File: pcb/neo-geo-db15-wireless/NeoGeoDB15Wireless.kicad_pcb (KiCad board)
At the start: 2 copper layers, 39.9 x 32 mm, 5 parts, among them J1 DB15_F, U1 RP2040-Zero, U2 NRF24L01

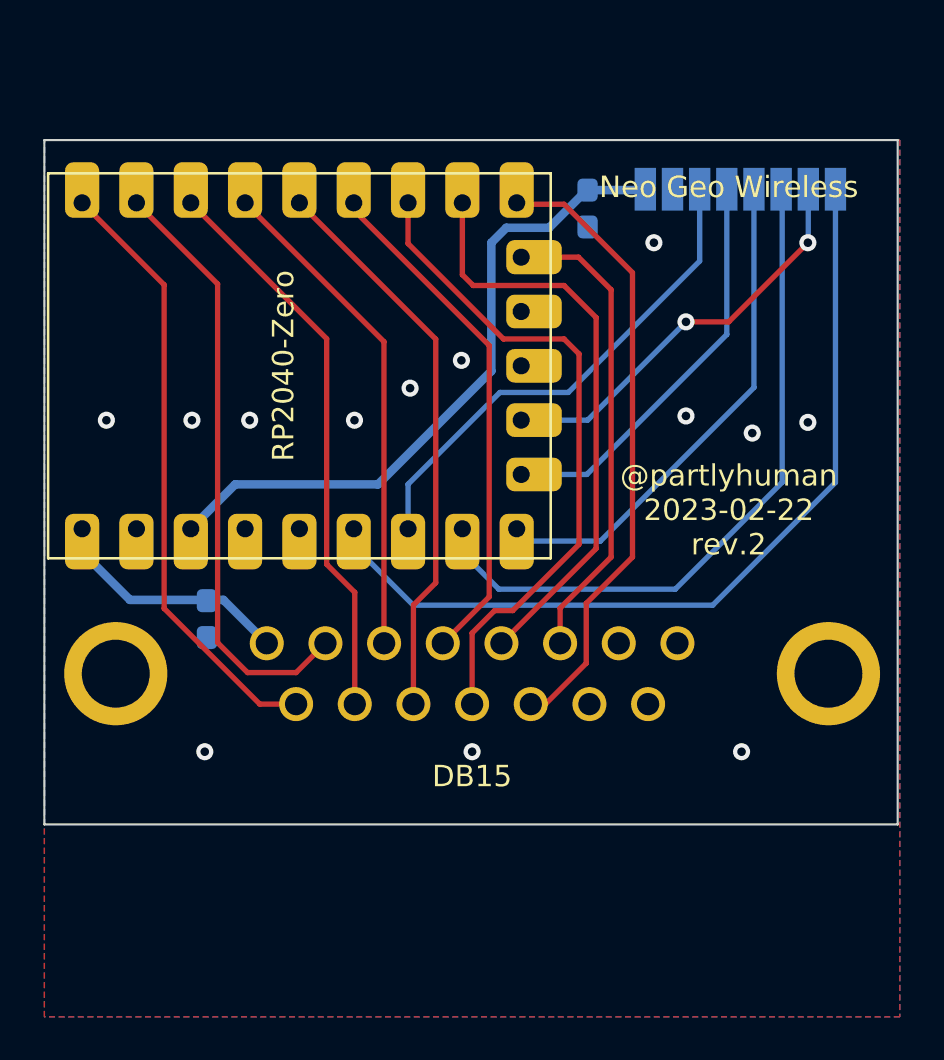
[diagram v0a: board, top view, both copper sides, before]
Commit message: Adds resistor packs for current limiting on button lines
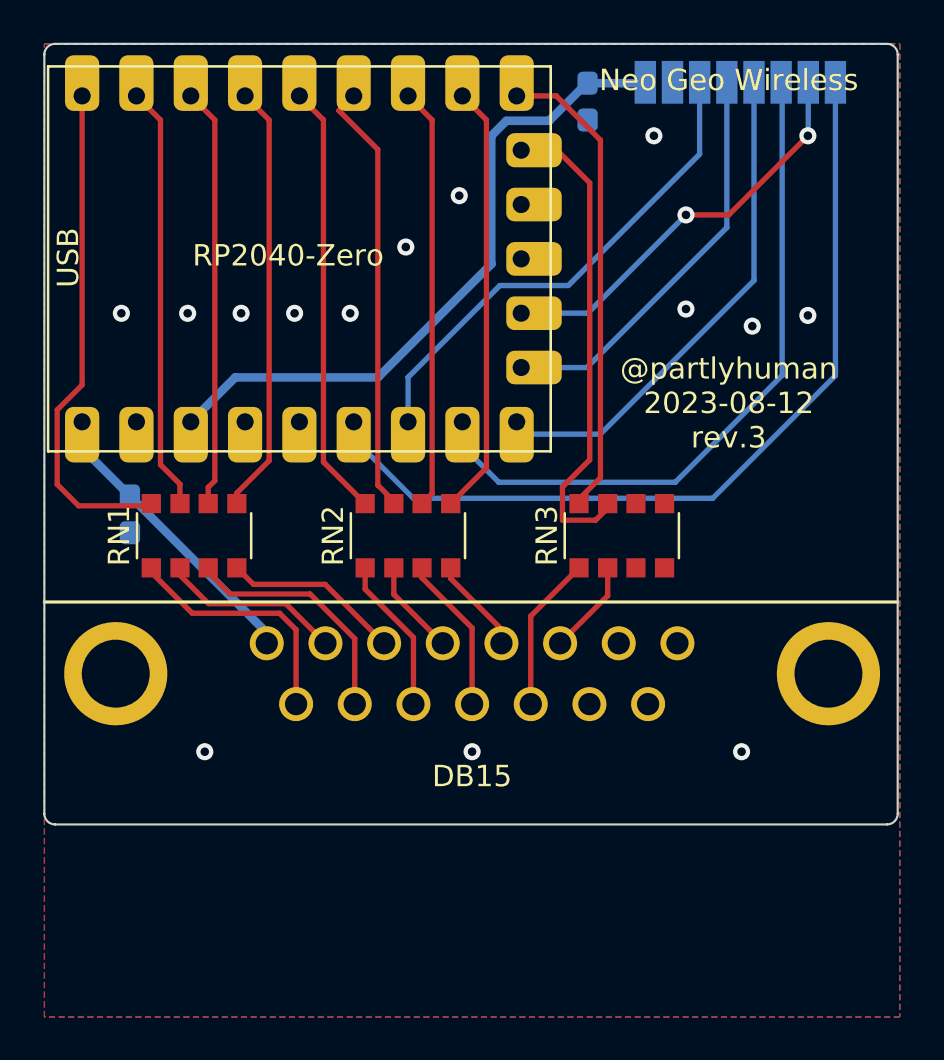
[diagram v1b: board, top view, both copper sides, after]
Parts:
- added RN1: R_Pack04, Resistor_SMD:R_Array_Convex_4x1206, F.Cu at (87.0, 80.0)
- added RN2: R_Pack04, Resistor_SMD:R_Array_Convex_4x1206, F.Cu at (97.0, 80.0)
- added RN3: R_Pack04, Resistor_SMD:R_Array_Convex_4x1206, F.Cu at (107.0, 80.0)
- moved C1 6.08 mm to (84.0, 79.0)
- moved C2 5.00 mm to (105.4, 59.7)
- moved U1 5.00 mm to (104.6, 77.2)
- moved U2 5.00 mm to (112.5, 67.5)
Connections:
- J1 pad 11: /STA -> /STA_IN
- J1 pad 12: /BC -> /BC_IN
- J1 pad 13: /BA -> /BA_IN
- J1 pad 14: /DL -> /DL_IN
- J1 pad 15: /DU -> /DU_IN
- J1 pad 3: /SEL -> /SEL_IN
- J1 pad 4: /BD -> /BD_IN
- J1 pad 5: /BB -> /BB_IN
- J1 pad 6: /DR -> /DR_IN
- J1 pad 7: /DD -> /DD_IN
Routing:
- net /DU_IN: track 0.00 -> 11.6 mm
- net /DL_IN: track 0.00 -> 11.4 mm
- net /BC: track 31.0 -> 19.7 mm
- net /DD_IN: track 0.00 -> 8.46 mm
- net /DD: track 28.3 -> 19.9 mm
- net /DR_IN: track 0.00 -> 8.35 mm
- net /BC_IN: track 0.00 -> 7.34 mm
- net /BA_IN: track 0.00 -> 7.31 mm
- net /STA_IN: track 0.00 -> 7.31 mm
- net /BD: track 27.5 -> 20.2 mm
- net /STA: track 29.3 -> 22.2 mm
- net /DL: track 26.6 -> 19.7 mm
- net /BA: track 26.5 -> 20.3 mm
- net /DU: track 28.6 -> 23.5 mm
- net /BD_IN: track 0.00 -> 4.51 mm
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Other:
- board size 39.9 x 32 mm -> 39.9 x 36.5 mm
- board text added: "USB"

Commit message: Add JLCJLCJLCJLC
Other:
- board text added: "JLCJLCJLCJLC"
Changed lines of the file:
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@@
     (effects (font (size 1 1) (thickness 0.15)))
+  )
+  (gr_text "JLCJLCJLCJLC" (at 80.8 92.9) (layer "F.SilkS")
+    (effects (font (size 0.8 0.8) (thickness 0.15)) (justify left bottom))
   )
   (gr_text "USB" (at 81.7 67 90) (layer "F.SilkS")

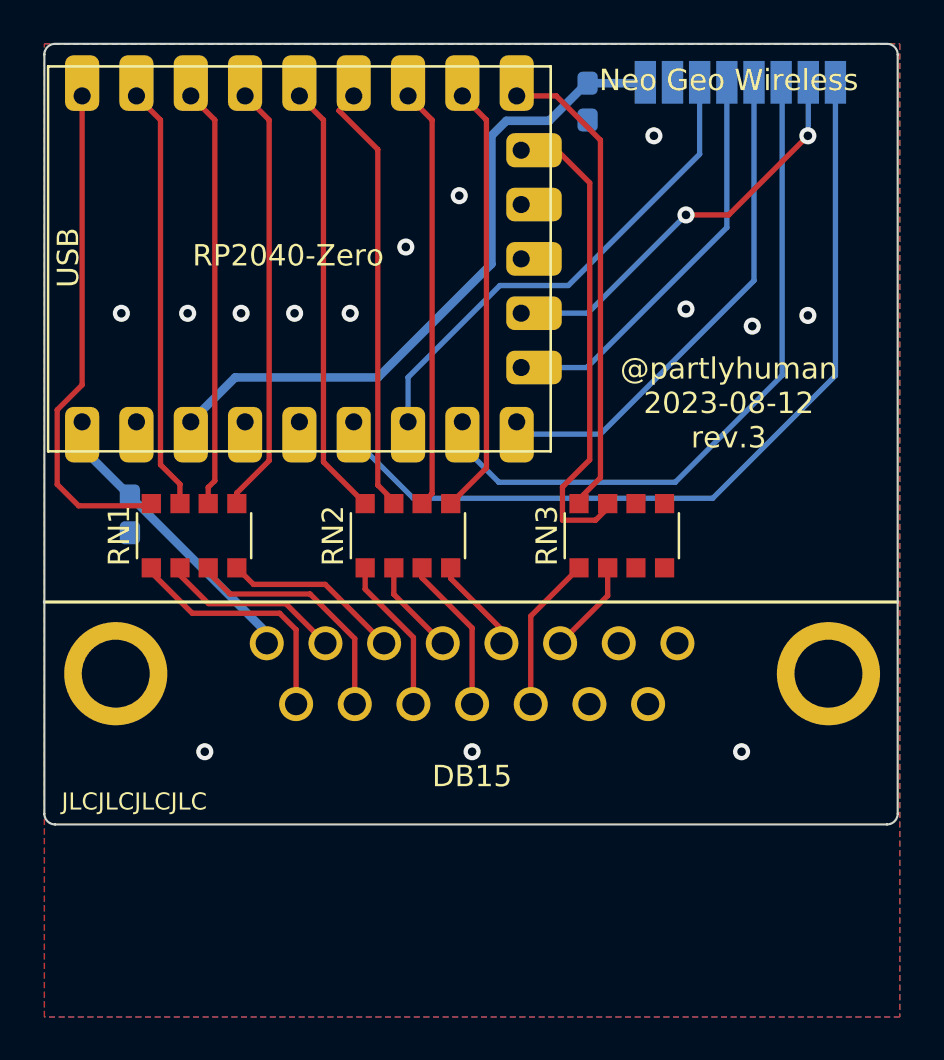
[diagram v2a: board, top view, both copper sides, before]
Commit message: Round size up to 40mm
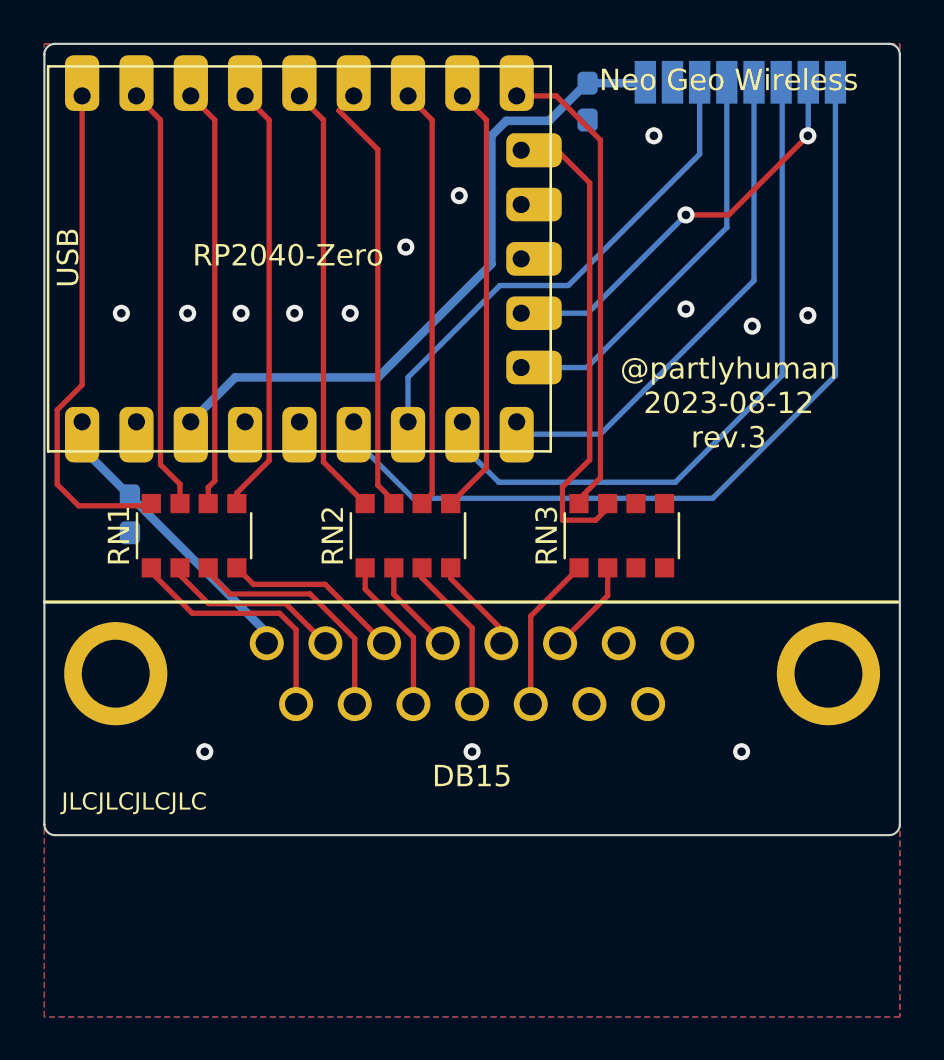
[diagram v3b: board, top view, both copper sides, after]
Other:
- board size 39.9 x 36.5 mm -> 40 x 37 mm
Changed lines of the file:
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@@
   (gr_line (start 80 83.1) (end 119.9 83.1)
     (stroke (width 0.15) (type default)) (layer "F.SilkS"))
-  (gr_arc (start 119.4 57) (mid 119.753553 57.146447) (end 119.9 57.5)
+  (gr_line (start 80.5 57) (end 119.5 57)
     (stroke (width 0.1) (type default)) (layer "Edge.Cuts"))
-  (gr_line (start 119.9 57.5) (end 119.9 93)
+  (gr_line (start 80 93.5) (end 80 57.5)
+    (stroke (width 0.1) (type default)) (layer "Edge.Cuts"))
+  (gr_line (start 119.5 94) (end 80.5 94)
     (stroke (width 0.1) (type default)) (layer "Edge.Cuts"))
   (gr_arc (start 80 57.5) (mid 80.146447 57.146447) (end 80.5 57)
     (stroke (width 0.1) (type default)) (layer "Edge.Cuts"))
-  (gr_arc (start 119.9 93) (mid 119.753553 93.353553) (end 119.4 93.5)
+  (gr_line (start 120 57.5) (end 120 93.5)
     (stroke (width 0.1) (type default)) (layer "Edge.Cuts"))
-  (gr_arc (start 80.5 93.5) (mid 80.146447 93.353553) (end 80 93)
+  (gr_arc (start 119.5 57) (mid 119.853553 57.146447) (end 120 57.5)
     (stroke (width 0.1) (type default)) (layer "Edge.Cuts"))
-  (gr_line (start 80 93) (end 80 57.5)
+  (gr_arc (start 120 93.5) (mid 119.853553 93.853553) (end 119.5 94)
     (stroke (width 0.1) (type default)) (layer "Edge.Cuts"))
-  (gr_line (start 119.4 93.5) (end 80.5 93.5)
-    (stroke (width 0.1) (type default)) (layer "Edge.Cuts"))
-  (gr_line (start 80.5 57) (end 119.4 57)
+  (gr_arc (start 80.5 94) (mid 80.146447 93.853553) (end 80 93.5)
     (stroke (width 0.1) (type default)) (layer "Edge.Cuts"))
   (gr_text "DB15" (at 100 91.25) (layer "F.SilkS")

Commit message: Voltage dividers on button inputs for pico safety
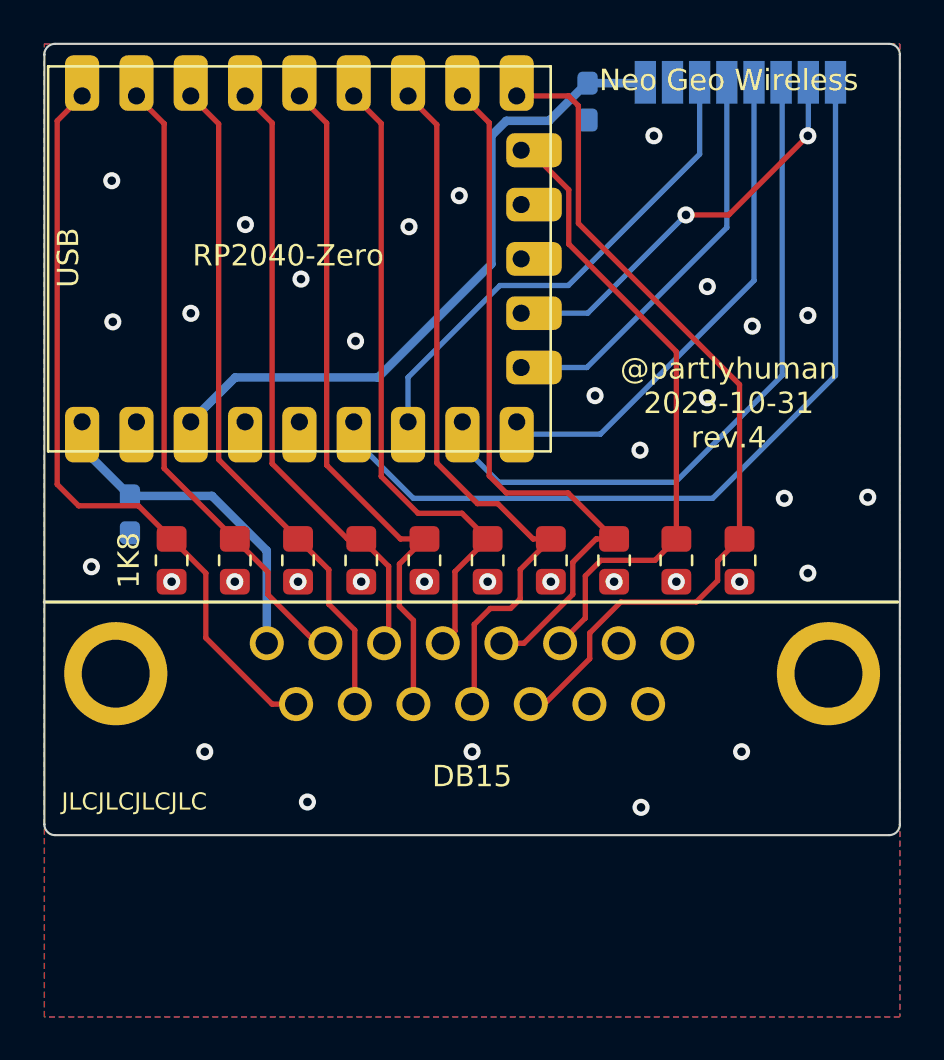
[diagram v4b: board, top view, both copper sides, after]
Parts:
- removed RN1, RN2, RN3: R_Pack04, Resistor_SMD:R_Array_Convex_4x1206
- added R1: 1K8, Resistor_SMD:R_0805_2012Metric_Pad1.20x1.40mm_HandSolder, F.Cu at (86.0, 81.2)
- added R10: 1K8, Resistor_SMD:R_0805_2012Metric_Pad1.20x1.40mm_HandSolder, F.Cu at (109.5, 81.2)
- added R2: 1K8, Resistor_SMD:R_0805_2012Metric_Pad1.20x1.40mm_HandSolder, F.Cu at (88.9, 81.2)
- added R3: 1K8, Resistor_SMD:R_0805_2012Metric_Pad1.20x1.40mm_HandSolder, F.Cu at (91.9, 81.2)
- added R4: 1K8, Resistor_SMD:R_0805_2012Metric_Pad1.20x1.40mm_HandSolder, F.Cu at (94.8, 81.2)
- added R5: 1K8, Resistor_SMD:R_0805_2012Metric_Pad1.20x1.40mm_HandSolder, F.Cu at (97.8, 81.2)
- added R6: 1K8, Resistor_SMD:R_0805_2012Metric_Pad1.20x1.40mm_HandSolder, F.Cu at (100.7, 81.2)
- added R7: 1K8, Resistor_SMD:R_0805_2012Metric_Pad1.20x1.40mm_HandSolder, F.Cu at (103.7, 81.2)
- added R8: 1K8, Resistor_SMD:R_0805_2012Metric_Pad1.20x1.40mm_HandSolder, F.Cu at (106.6, 81.2)
- added R9: 1K8, Resistor_SMD:R_0805_2012Metric_Pad1.20x1.40mm_HandSolder, F.Cu at (112.5, 81.2)
- U2: value NRF24L01 -> NRF24L01_Breakout
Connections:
- J1 pad 11: /STA_IN -> /STA
- J1 pad 12: /BC_IN -> /BC
- J1 pad 13: /BA_IN -> /BA
- J1 pad 14: /DL_IN -> /DL
- J1 pad 15: /DU_IN -> /DU
- J1 pad 3: /SEL_IN -> /SEL
- J1 pad 4: /BD_IN -> /BD
- J1 pad 5: /BB_IN -> /BB
- J1 pad 6: /DR_IN -> /DR
- J1 pad 7: /DD_IN -> /DD
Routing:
- net /STA: track 22.2 -> 40.7 mm
- net /BC: track 19.7 -> 34.3 mm
- net /BD: track 20.2 -> 33.5 mm
- net /DU: track 23.5 -> 35.8 mm
- net /DL: track 19.7 -> 31.6 mm
- net /BA: track 20.3 -> 32.3 mm
- net /DU_IN: track 11.6 -> 0.00 mm
- net /DL_IN: track 11.4 -> 0.00 mm
- net /BB: track 20.4 -> 30.3 mm
- net /DD: track 19.9 -> 29.5 mm
- net /DR: track 20.2 -> 28.8 mm
- net /DD_IN: track 8.46 -> 0.00 mm
- net /DR_IN: track 8.35 -> 0.00 mm
- net /BC_IN: track 7.34 -> 0.00 mm
- net /SEL: track 22.7 -> 30.0 mm
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
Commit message: Rev4 wireless board with voltage dividers
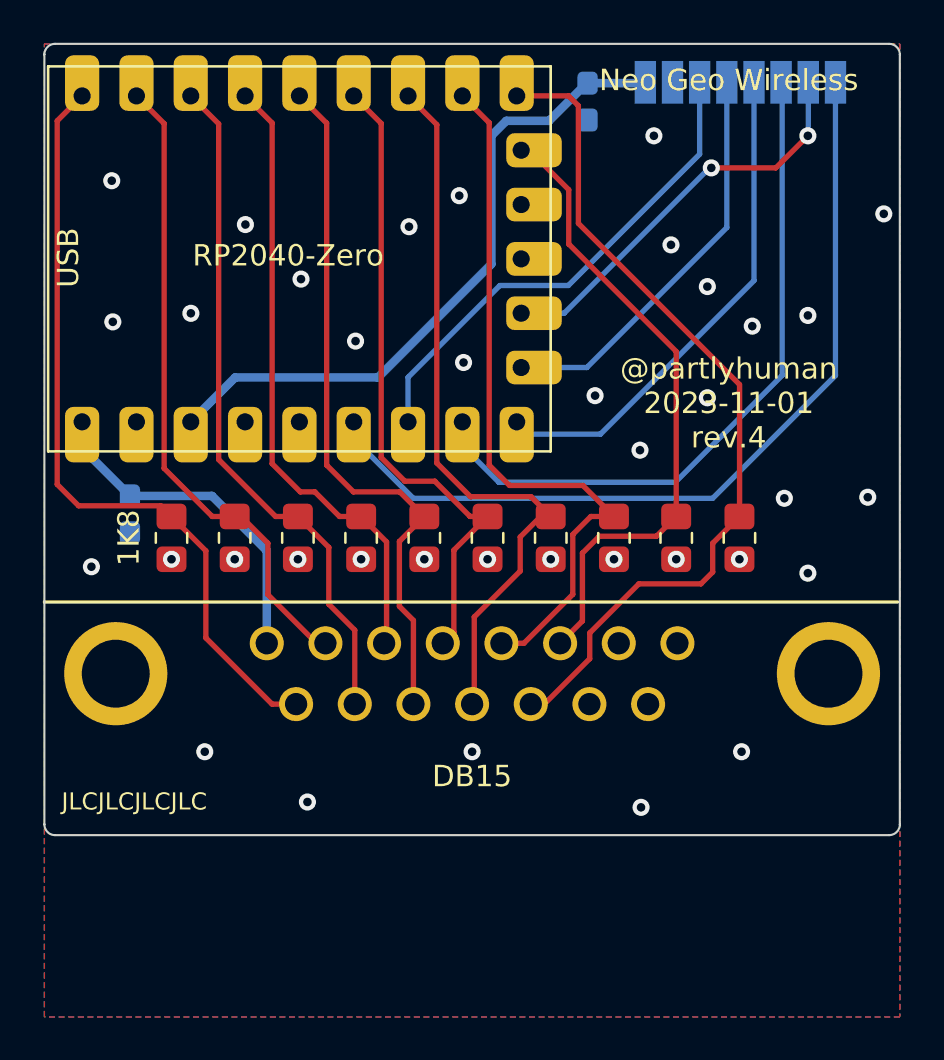
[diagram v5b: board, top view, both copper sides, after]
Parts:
- moved R1 1.05 mm to (85.9, 80.1)
- moved R10 1.05 mm to (109.5, 80.1)
- moved R2 1.05 mm to (88.9, 80.1)
- moved R3 1.05 mm to (91.9, 80.1)
- moved R4 1.05 mm to (94.8, 80.1)
- moved R5 1.05 mm to (97.8, 80.1)
- moved R6 1.05 mm to (100.7, 80.1)
- moved R7 1.05 mm to (103.7, 80.1)
- moved R8 1.05 mm to (106.6, 80.1)
- moved R9 1.05 mm to (112.5, 80.1)
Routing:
- net /DD: track 29.5 -> 30.3 mm
- net /DU: track 35.8 -> 36.5 mm
- net /DL: track 31.6 -> 32.2 mm
- net /DR: track 28.8 -> 29.4 mm
- net GND: vias 34 -> 37

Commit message: Use 0805 capacitors
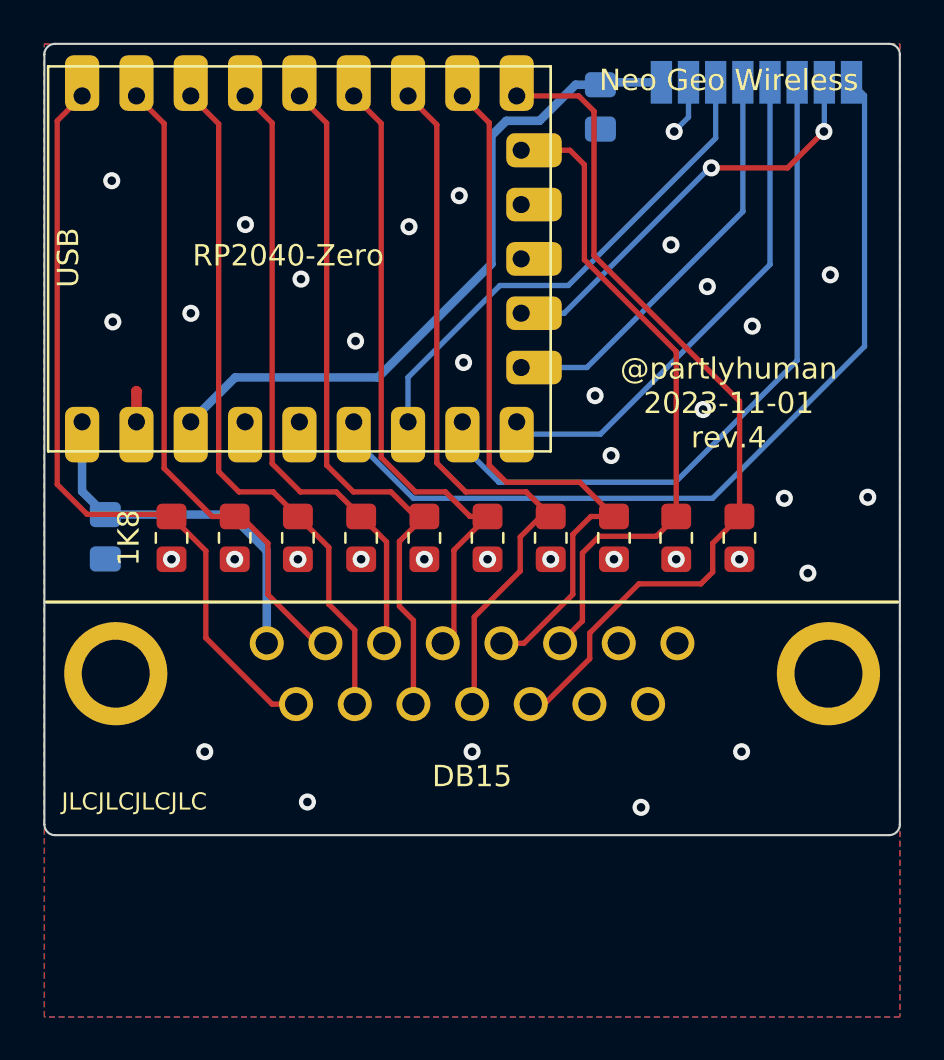
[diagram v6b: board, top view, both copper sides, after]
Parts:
- C1, C2: footprint Capacitor_SMD:C_0603_1608Metric_Pad1.08x0.95mm_HandSolder -> Capacitor_SMD:C_0805_2012Metric_Pad1.18x1.45mm_HandSolder
- moved C1 1.56 mm to (82.8, 80.0)
- moved U2 0.75 mm to (113.2, 67.5)
- moved C2 0.65 mm to (106.0, 60.0)
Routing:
- net GND: track 0.00 -> 4.00 mm, vias 37 -> 35
- net /VCC: track 16.2 -> 17.4 mm
- net /SEL: track 30.1 -> 31.2 mm
- net /IRQ: track 40.6 -> 41.4 mm
- net /3V3: track 31.3 -> 32.1 mm
- net /MISO: track 19.3 -> 20.0 mm
